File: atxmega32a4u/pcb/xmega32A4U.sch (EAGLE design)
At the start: 14 parts

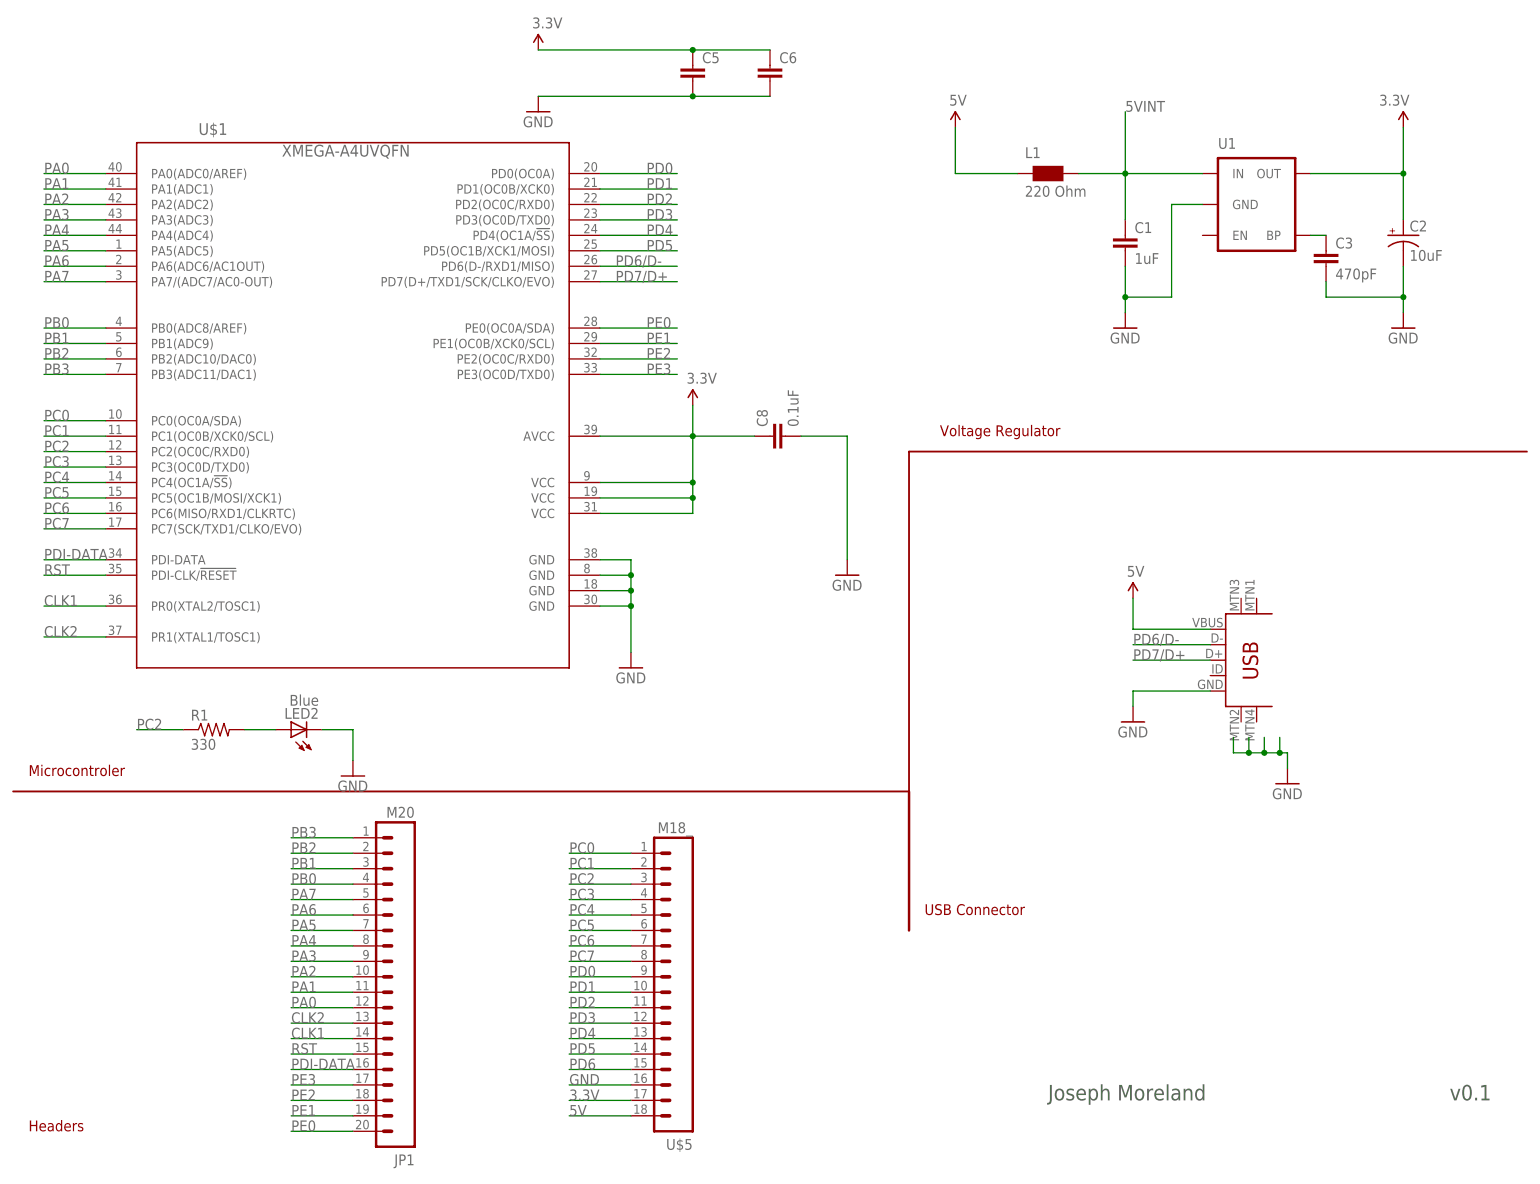
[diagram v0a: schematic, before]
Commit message: Fix ciruit errors in LDO, added ESD protection to USB circuit - this will be v0.3
v0.3 ready
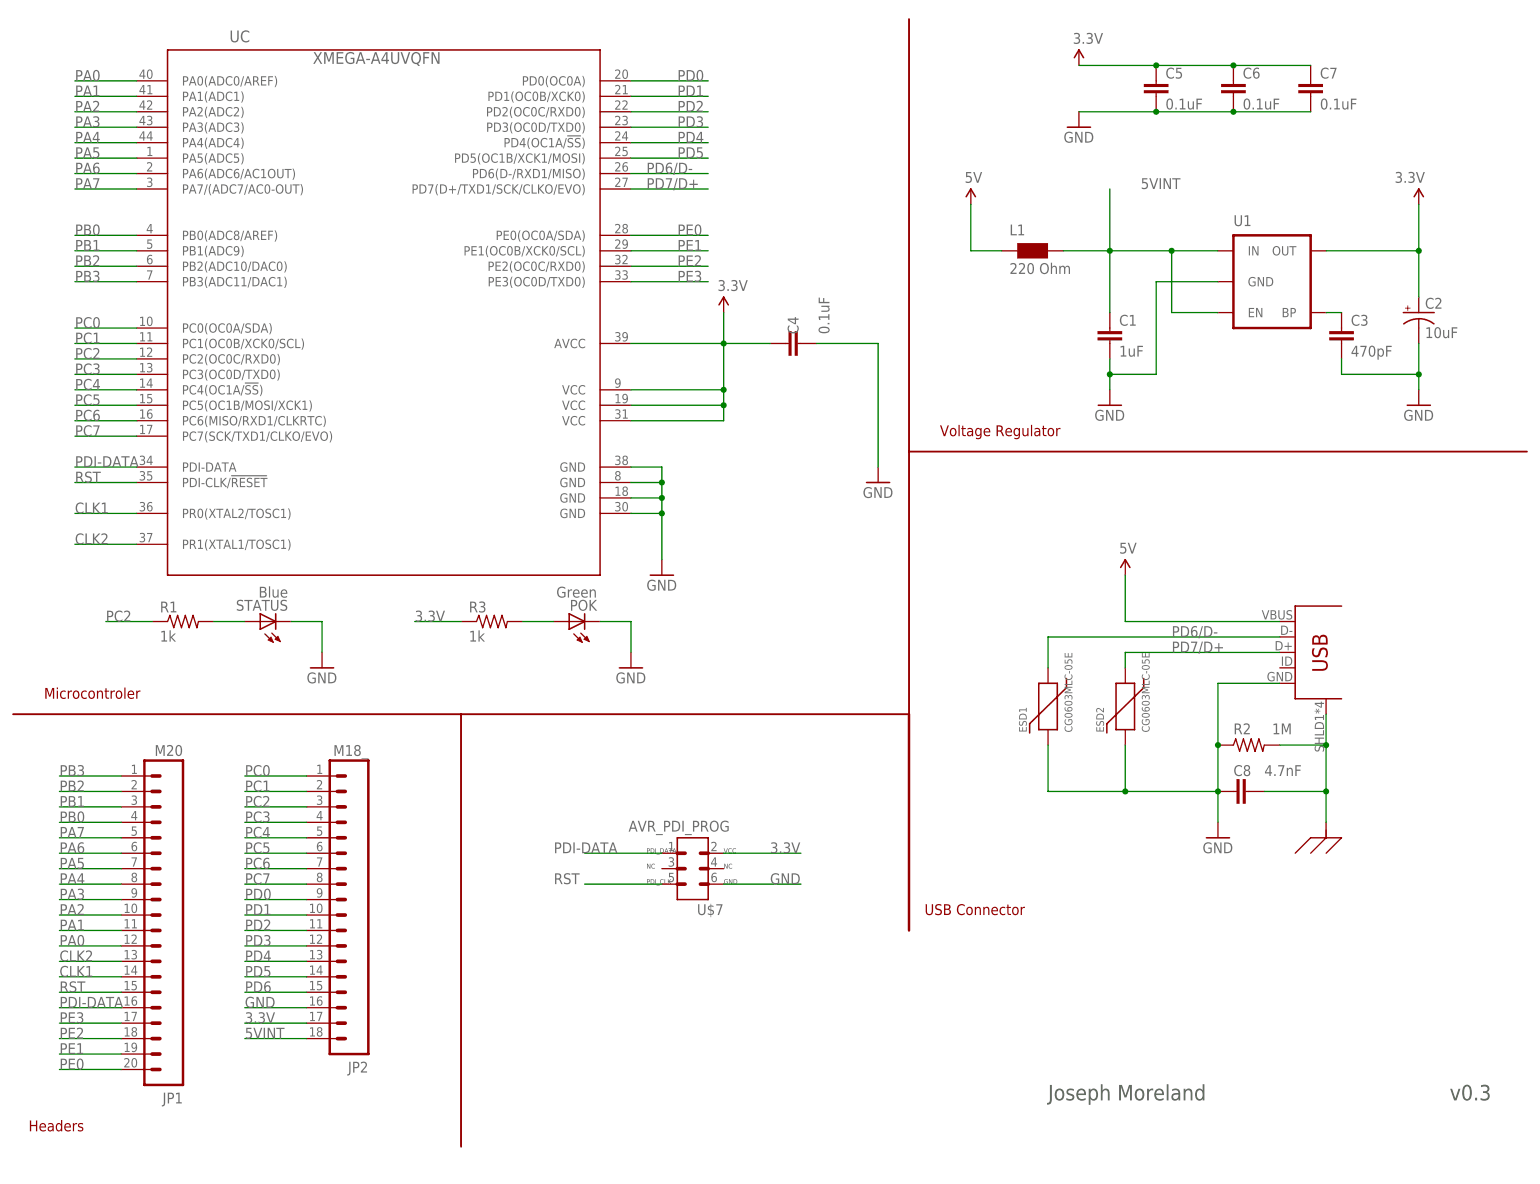
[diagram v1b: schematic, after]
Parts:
- removed LED2: Blue, SparkFun-LED:LED0603
- removed U$1: XMEGA-A4UVQFN, JCM:XMEGA-A4UVQFN
- removed U$5: M18_, SparkFun-Connectors:M18_
- added C4, C7: 0.1uF, SparkFun-Capacitors:CAP0402-CAP
- added ESD1, ESD2: CG0603MLC-05E, JCM:CG0603MLC
- added JP2: M18_, SparkFun-Connectors:M18_
- added POK: Green, SparkFun-LED:LED0603
- added R2: 1M, SparkFun-Resistors:RESISTOR0402-RES
- added R3: 1k, SparkFun-Passives:RESISTOR0603-RES
- added STATUS: Blue, SparkFun-LED:LED0603
- added U$7: AVR_PDI_PROG, JCM:AVR_PDI_PROG
- added UC: XMEGA-A4UVQFN, JCM:XMEGA-A4UVQFN
- C1: device rcl:C-EUC0603 -> SparkFun-Capacitors:CAP0603-CAP; PARTNO (none) -> C0603C105K3PACTU
- C2: device SparkFun-Passives:CAP_POL1206 -> SparkFun-Capacitors:CAP_POL1206; PARTNO (none) -> T494A106M020AT
- C3: device rcl:C-EUC0603 -> SparkFun-Capacitors:CAP0603-CAP; PARTNO (none) -> C0603C471K5RACTU
- C5, C6: value (none) -> 0.1uF; device SparkFun-Passives:CAP0402-CAP -> SparkFun-Capacitors:CAP0402-CAP; PARTNO (none) -> GMK105BJ104KV-F
- C8: value 0.1uF -> 4.7nF; device rcl:C-EUC0402 -> SparkFun-Capacitors:CAP0402-CAP
- JP1: PARTNO (none) -> M20-9732046
- L1: PARTNO (none) -> MPZ1608S221A
- R1: value 330 -> 1k; device adafruit:R-US_R0603 -> SparkFun-Passives:RESISTOR0603-RES; PARTNO (none) -> RC0603FR-07330RL
- U$4: value USB-MINIB-5PIN -> USB-MINIB; device SparkFun-Connectors:USB-MINIB-5PIN -> JCM-Connectors:USB-MINIB; PARTNO (none) -> USB-M26FTR
- U1: PARTNO (none) -> MIC5219-3.3YM5 TR
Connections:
- new net N$1: POK.A, R3.2
- new net SHLD: C8.2, R2.2, U$4.SHLD
- net 3.3V: now also C4.1, C7.1, JP2.17, R3.1, U$7.VCC, UC.AVCC, UC.VCC@1, UC.VCC@2, UC.VCC@3; no longer C8.1, U$1.AVCC, U$1.VCC@1, U$1.VCC@2, U$1.VCC@3, U$5.17
- net 5V: no longer U$5.18
- net 5VINT: now also JP2.18, U1.EN
- net CLK1: now also UC.PR0(XTAL2/TOSC1); no longer U$1.PR0(XTAL2/TOSC1)
- net CLK2: now also UC.PR1(XTAL1/TOSC1); no longer U$1.PR1(XTAL1/TOSC1)
- net GND: now also C4.2, C7.2, C8.1, ESD1.P$1, ESD2.P$1, JP2.16, POK.C, R2.1, STATUS.C, U$7.GND, UC.GND@1, UC.GND@2, UC.GND@3, UC.GND@4; no longer C8.2, LED2.C, U$1.GND@1, U$1.GND@2, U$1.GND@3, U$1.GND@4, U$5.16
- net N$2: now also STATUS.A; no longer LED2.A
- net PA0: now also UC.PA0(ADC0/AREF); no longer U$1.PA0(ADC0/AREF)
- net PA1: now also UC.PA1(ADC1); no longer U$1.PA1(ADC1)
- net PA2: now also UC.PA2(ADC2); no longer U$1.PA2(ADC2)
- net PA3: now also UC.PA3(ADC3); no longer U$1.PA3(ADC3)
- net PA4: now also UC.PA4(ADC4); no longer U$1.PA4(ADC4)
- net PA5: now also UC.PA5(ADC5); no longer U$1.PA5(ADC5)
- net PA6: now also UC.PA6(ADC6/AC1OUT); no longer U$1.PA6(ADC6/AC1OUT)
- net PA7: now also UC.PA7/(ADC7/AC0-OUT); no longer U$1.PA7/(ADC7/AC0-OUT)
- net PB0: now also UC.PB0(ADC8/AREF); no longer U$1.PB0(ADC8/AREF)
- net PB1: now also UC.PB1(ADC9); no longer U$1.PB1(ADC9)
- net PB2: now also UC.PB2(ADC10/DAC0); no longer U$1.PB2(ADC10/DAC0)
- net PB3: now also UC.PB3(ADC11/DAC1); no longer U$1.PB3(ADC11/DAC1)
- net PC0: now also JP2.1, UC.PC0(OC0A/SDA); no longer U$1.PC0(OC0A/SDA), U$5.1
- net PC1: now also JP2.2, UC.PC1(OC0B/XCK0/SCL); no longer U$1.PC1(OC0B/XCK0/SCL), U$5.2
- net PC2: now also JP2.3, UC.PC2(OC0C/RXD0); no longer U$1.PC2(OC0C/RXD0), U$5.3
- net PC3: now also JP2.4, UC.PC3(OC0D/TXD0); no longer U$1.PC3(OC0D/TXD0), U$5.4
- net PC4: now also JP2.5, UC.PC4(OC1A/!SS!); no longer U$1.PC4(OC1A/!SS!), U$5.5
- net PC5: now also JP2.6, UC.PC5(OC1B/MOSI/XCK1); no longer U$1.PC5(OC1B/MOSI/XCK1), U$5.6
- net PC6: now also JP2.7, UC.PC6(MISO/RXD1/CLKRTC); no longer U$1.PC6(MISO/RXD1/CLKRTC), U$5.7
- net PC7: now also JP2.8, UC.PC7(SCK/TXD1/CLKO/EVO); no longer U$1.PC7(SCK/TXD1/CLKO/EVO), U$5.8
- net PD0: now also JP2.9, UC.PD0(OC0A); no longer U$1.PD0(OC0A), U$5.9
- net PD1: now also JP2.10, UC.PD1(OC0B/XCK0); no longer U$1.PD1(OC0B/XCK0), U$5.10
- net PD2: now also JP2.11, UC.PD2(OC0C/RXD0); no longer U$1.PD2(OC0C/RXD0), U$5.11
- net PD3: now also JP2.12, UC.PD3(OC0D/TXD0); no longer U$1.PD3(OC0D/TXD0), U$5.12
- net PD4: now also JP2.13, UC.PD4(OC1A/!SS!); no longer U$1.PD4(OC1A/!SS!), U$5.13
- net PD5: now also JP2.14, UC.PD5(OC1B/XCK1/MOSI); no longer U$1.PD5(OC1B/XCK1/MOSI), U$5.14
- net PD6: now also JP2.15; no longer U$5.15
- net PD6/D-: now also ESD1.P$2, UC.PD6(D-/RXD1/MISO); no longer U$1.PD6(D-/RXD1/MISO)
- net PD7/D+: now also ESD2.P$2, UC.PD7(D+/TXD1/SCK/CLKO/EVO); no longer U$1.PD7(D+/TXD1/SCK/CLKO/EVO)
- net PDI-DATA: now also U$7.PDI_DATA, UC.PDI-DATA; no longer U$1.PDI-DATA
- net PE0: now also UC.PE0(OC0A/SDA); no longer U$1.PE0(OC0A/SDA)
- net PE1: now also UC.PE1(OC0B/XCK0/SCL); no longer U$1.PE1(OC0B/XCK0/SCL)
- net PE2: now also UC.PE2(OC0C/RXD0); no longer U$1.PE2(OC0C/RXD0)
- net PE3: now also UC.PE3(OC0D/TXD0); no longer U$1.PE3(OC0D/TXD0)
- net RST: now also U$7.PDI_CLK, UC.PDI-CLK/!RESET; no longer U$1.PDI-CLK/!RESET
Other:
- note added: "v0.3"
- note removed: "v0.1"
- moved on the sheet: C1, C2, C3, C5, C6, C8, JP1, L1, R1, U1
